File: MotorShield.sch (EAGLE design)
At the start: 125 parts, among them IC1 OPA4340E, IC2 OPA4340E, IC3 74HCT125D, IC4 MCP3008SL, T1 FDN337N, T2 FDN337N, T3 FDN337N, T4 FDN337N, T5 FDN337N, T6 FDN337N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

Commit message: added button led reordered device names
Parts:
- added LED18: yellow, led:LEDCHIP-LED0805
- added R62: 10k, rcl:R-EU_R0805
- R10, R13, R16: value 100k -> 10k
- R12, R15, R9: value 100m -> 10k
- R17, R19, R21, R23: value 27k -> 100k
- R18, R20, R22, R24: value 1k -> 100k
- R2, R4, R7: value 100k -> 100m
- R25, R27, R29, R31: value 27k -> 1k
- R33, R34, R37, R40: value 10k -> 27k
- R35, R38: value 100m -> 27k
- R36, R39: value 100k -> 27k
- R5, R8: value 10k -> 100m
- R57: value 10k -> 2k2
- R58: value 220 -> 2k2
- R61: value 2k2 -> 220
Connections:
- removed net 24V/1A: D1.C, F1.1, LED1.C, X2-1.1
- new net D8: D8.C, F8.1, LED1.C, X2-1.1
- new net N$63: LED18.A, R57.1
- net +24V: now also R57.2, R58.2; no longer R61.2
- net BTN_LED: now also R62.2; no longer R57.2
- net CH0: now also R33.2; no longer R21.2
- net CH1: now also R34.2; no longer R23.2
- net CH2: now also R35.2; no longer R19.2
- net CH3: now also R36.2; no longer R17.2
- net CH4: now also R37.2; no longer R29.2
- net CH5: now also R38.2; no longer R31.2
- net CH6: now also R39.2; no longer R25.2
- net CH7: now also R40.2; no longer R27.2
- net GND: now also R10.1, R13.1, R16.1, R2.1, R25.1, R27.1, R29.1, R31.1, R4.1, R61.1, R62.1, R7.1; no longer R18.1, R20.1, R22.1, R24.1, R33.1, R34.1, R35.1, R37.1, R38.1, R40.1, R57.1, R58.1
- net M0: now also R9.2, T1.G; no longer R40.2, T8.G
- net M1: now also R10.2, T2.G; no longer R37.2, T7.G
- net M2: now also R11.2, T3.G; no longer R34.2, T6.G
- net M3: now also R12.2, T4.G; no longer R14.2, T5.G
- net M4: now also R13.2, T5.G; no longer R11.2, T4.G
- net M5: now also R14.2, T6.G; no longer R8.2, T3.G
- net M6: now also R15.2, T7.G; no longer R5.2, T2.G
- net M7: now also R16.2, T8.G; no longer R33.2, T1.G
- net N$10: now also D7.A, T7.D; no longer D2.A, T2.D
- net N$11: now also R23.1, R7.2, T7.S; no longer R3.2, R4.1, T2.S
- net N$12: now also D6.C, F6.1; no longer D3.C, F3.1
- net N$13: now also D7.C, F7.1; no longer D2.C, F2.1
- net N$15: now also R28.2, R36.1; no longer R17.1, R18.2
- net N$17: now also D6.A, T6.D; no longer D3.A, T3.D
- net N$18: now also R22.1, T6.S; no longer R7.1, T3.S
- net N$2: now also D8.A, T8.D; no longer D1.A, T1.D
- net N$22: now also R25.2, R33.1; no longer R21.1, R22.2
- net N$26: now also D5.A, T5.D; no longer D4.A, T4.D
- net N$27: now also R26.2, R34.1; no longer R23.1, R24.2
- net N$29: now also R21.1, R5.2, T5.S; no longer R10.1, R9.2, T4.S
- net N$3: now also R24.1, R8.2, T8.S; no longer R1.2, R2.1, T1.S
- net N$31: now also R31.2, R39.1; no longer R25.1, R26.2
- net N$32: now also LED18.C
- net N$33: now also R59.2; no longer R58.2
- net N$34: now also R32.2, R40.1; no longer R27.1, R28.2
- net N$37: now also R29.2, R37.1; no longer R29.1, R30.2
- net N$38: now also D4.A, T4.D; no longer D5.A, T5.D
- net N$39: now also R20.1, R4.2, T4.S; no longer R12.2, R13.1, T5.S
- net N$4: now also D1.C, F1.1; no longer D8.C, F8.1
- net N$40: now also R30.2, R38.1; no longer R31.1, R32.2
- net N$45: now also D3.A, T3.D; no longer D6.A, T6.D
- net N$46: now also R19.1, R3.2, T3.S; no longer R15.2, R16.1, T6.S
- net N$5: now also D2.C, F2.1; no longer D7.C, F7.1
- net N$51: now also D2.A, T2.D; no longer D7.A, T7.D
- net N$52: now also R18.1, R2.2, T2.S; no longer R35.2, R36.1, T7.S
- net N$57: now also D1.A, T1.D; no longer D8.A, T8.D
- net N$58: now also R1.2, R17.1, T1.S; no longer R38.2, R39.1, T8.S
- net N$6: now also R27.2, R35.1; no longer R19.1, R20.2
- net N$60: now also R60.2; no longer R59.2
- net N$61: now also R61.2; no longer R60.2
- net N$62: now also R58.1; no longer R61.1
- net N$7: now also D3.C, F3.1; no longer D6.C, F6.1
- net N$8: now also D4.C, F4.1; no longer D5.C, F5.1
- net N$9: now also D5.C, F5.1; no longer D4.C, F4.1
- net V0: now also C1.1, R17.2; no longer C8.1, R39.2
- net V1: now also C2.1, R18.2; no longer C7.1, R36.2
- net V2: now also C3.1, R19.2; no longer C6.1, R16.2
- net V3: now also C4.1, R20.2; no longer C5.1, R13.2
- net V4: now also C5.1, R21.2; no longer C4.1, R10.2
- net V5: now also C6.1, R22.2; no longer C3.1, R7.2
- net V6: now also C7.1, R23.2; no longer C2.1, R4.2
- net V7: now also C8.1, R24.2; no longer C1.1, R2.2
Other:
- moved on the sheet: C1, C2, C3, C4, C5, C6, C7, C8, D1, D2, D3, D4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

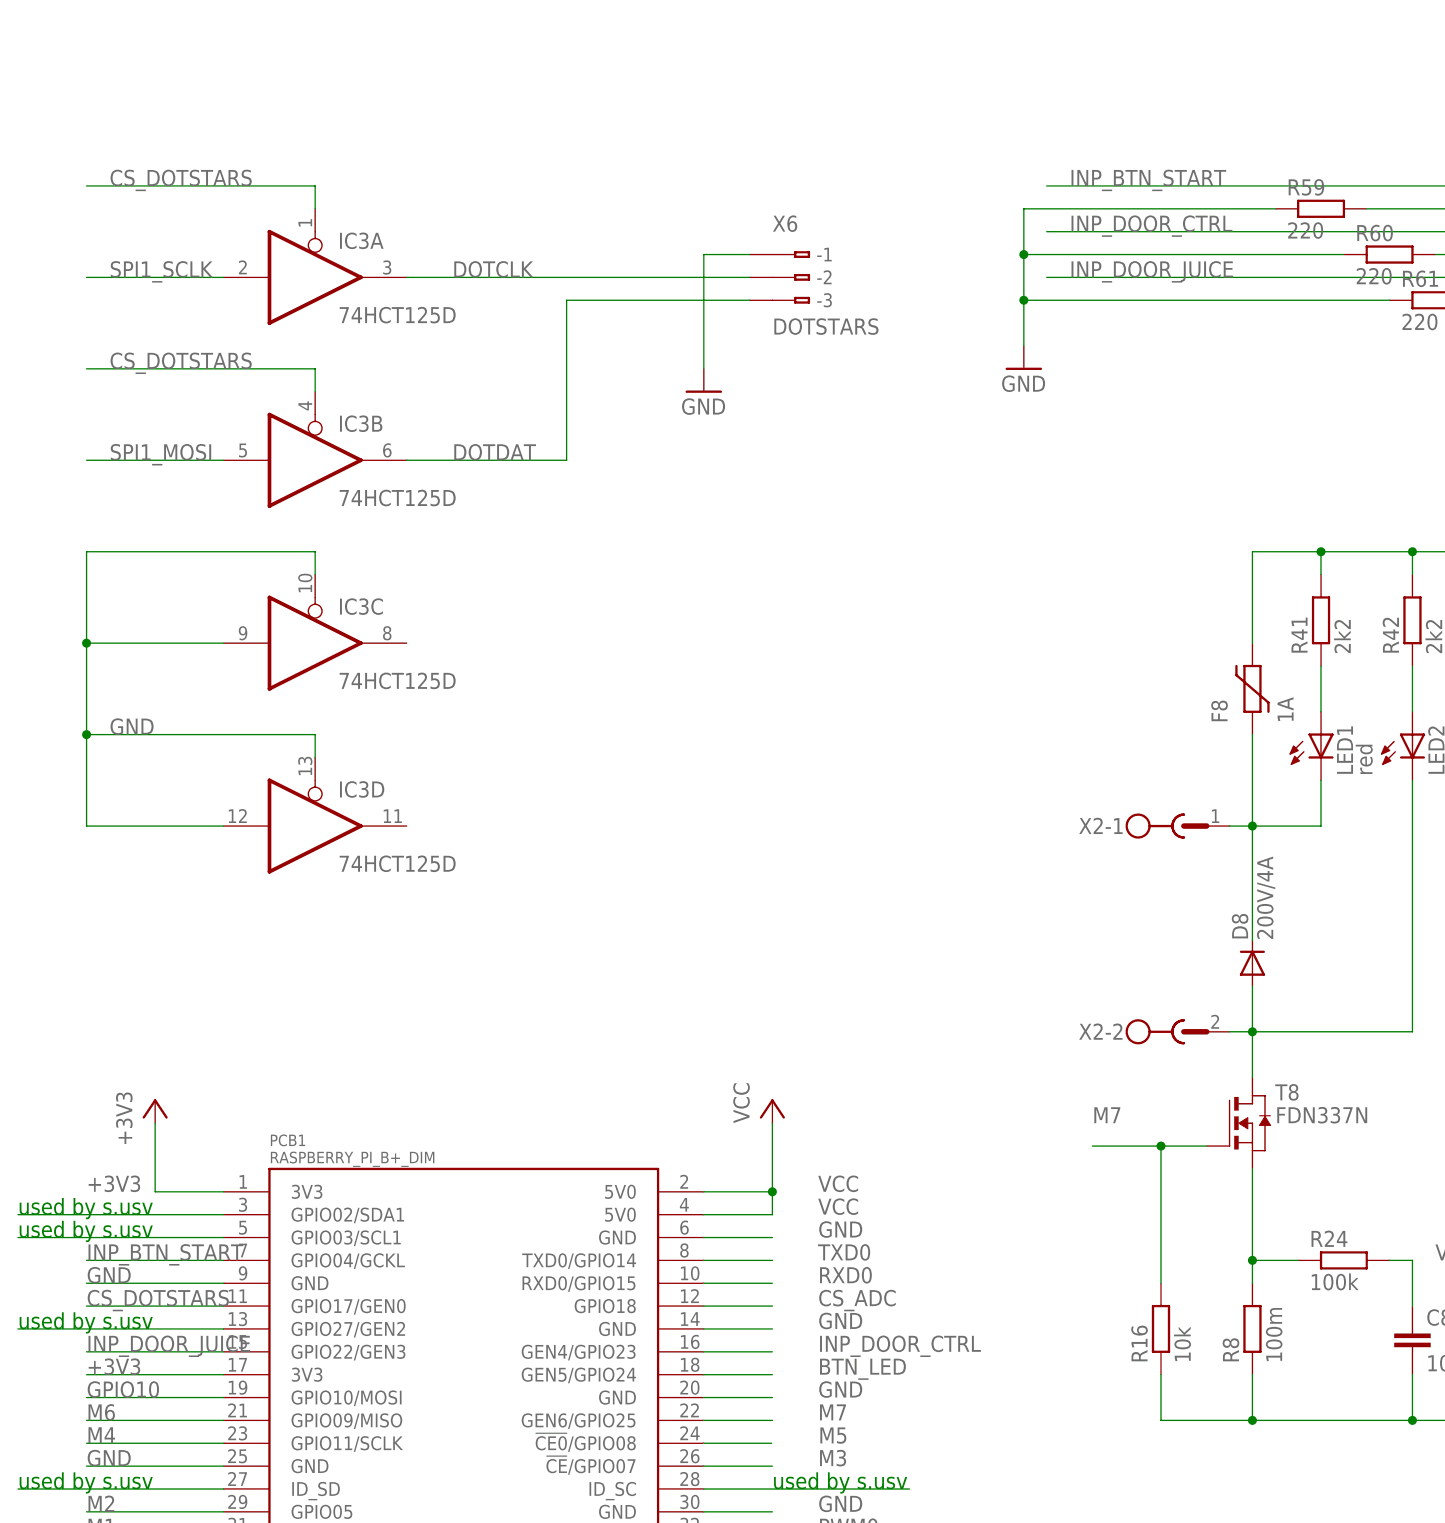
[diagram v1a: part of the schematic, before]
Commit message: Moved input for start button near to X5. #24
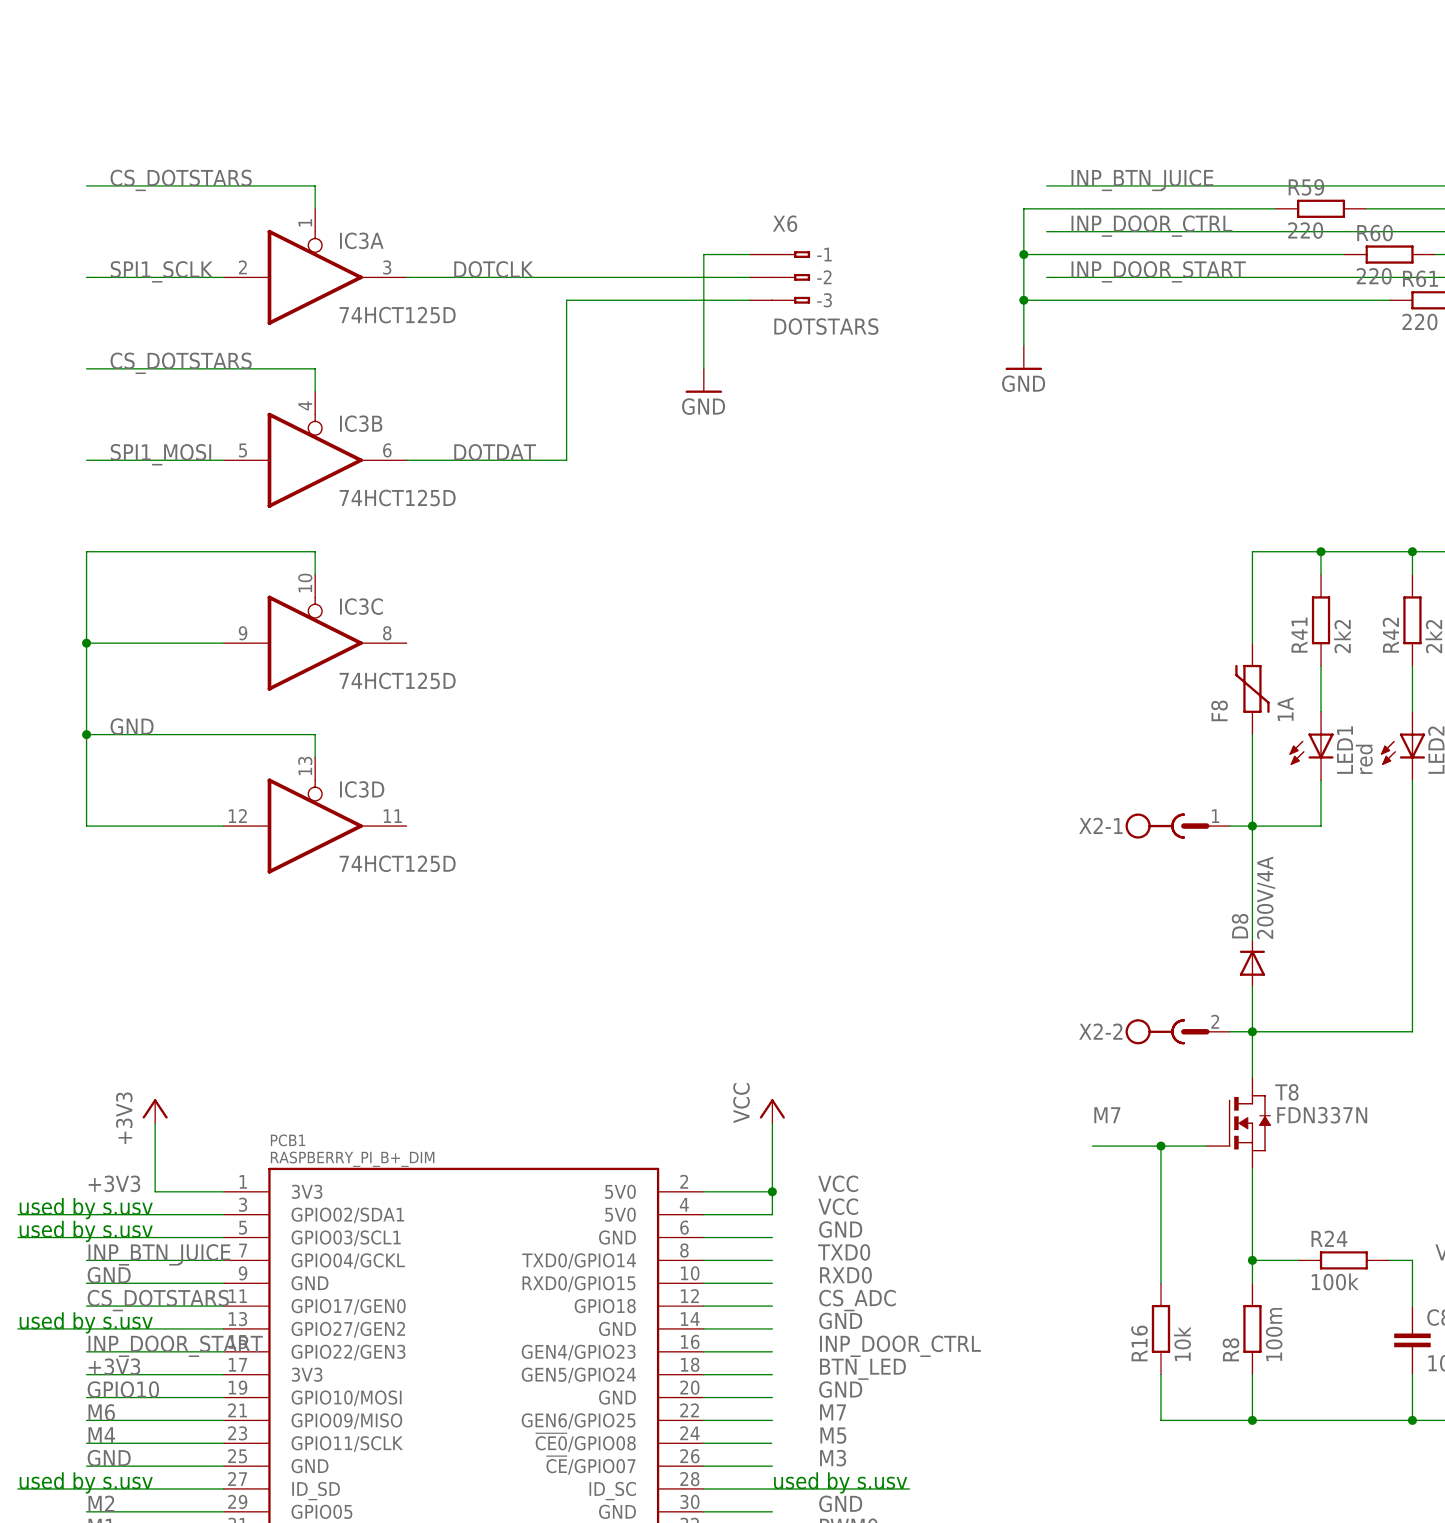
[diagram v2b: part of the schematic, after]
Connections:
- net INP_BTN_START renamed INP_BTN_JUICE
- net INP_DOOR_JUICE renamed INP_DOOR_START
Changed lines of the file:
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@@
 </segment>
 </net>
-<net name="INP_BTN_START" class="0">
+<net name="INP_BTN_JUICE" class="0">
 <segment>
 <wire x1="137.16" y1="198.12" x2="86.36" y2="198.12" width="0.1524" layer="91"/>
@@
 </segment>
 </net>
-<net name="INP_DOOR_JUICE" class="0">
+<net name="INP_DOOR_START" class="0">
 <segment>
 <wire x1="137.16" y1="187.96" x2="86.36" y2="187.96" width="0.1524" layer="91"/>
